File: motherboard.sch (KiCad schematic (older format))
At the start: 91 parts, among them P1 CONN_01X08, P2 CONN_01X08, U1 STM32F411-LQFP64, U10 74LS125, U11 74LS125, U12 74LS125, U13 74LS125, U14 74LS125, U15 PCA9517A, U16 PCA9517A, U2 STM32F411-LQFP64, U3 AP7313, U4 74LVC2G132, U5 FM25V20A-G, U6 FM25V20A-G, U7 FM25V20A-G, U8 FM25V20A-G, U9 74LS125, Y1 32k, Y2 8M(16pF), Y3 32k, Y4 8M(16pF)

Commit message: Added radio interrupt lines
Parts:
- removed P?: CONN_02X03, symbol CONN_02X03
- added U17: 74LS125, symbol 74LS125
- gave numbers to parts that had none: 2
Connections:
- net labels added: RADIO_RR, RADIO_RR_P, RADIO_RR_S, RADIO_TR, RADIO_TR_P, RADIO_TR_S, SGPIO_4, SGPIO_5
- net labels removed: DEP_C, DEP_NC, DEP_NO, GPIO13, GPIO14, RBF_C, RBF_NC, RBF_NO, SGPIO14, SGPIO15, SGPIO4, SGPIO5
- wire segments 264 -> 394
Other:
- moved on the sheet: C23, C24, C25, C26, P3, P4, R10, R11, R12, R13, R23, R24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

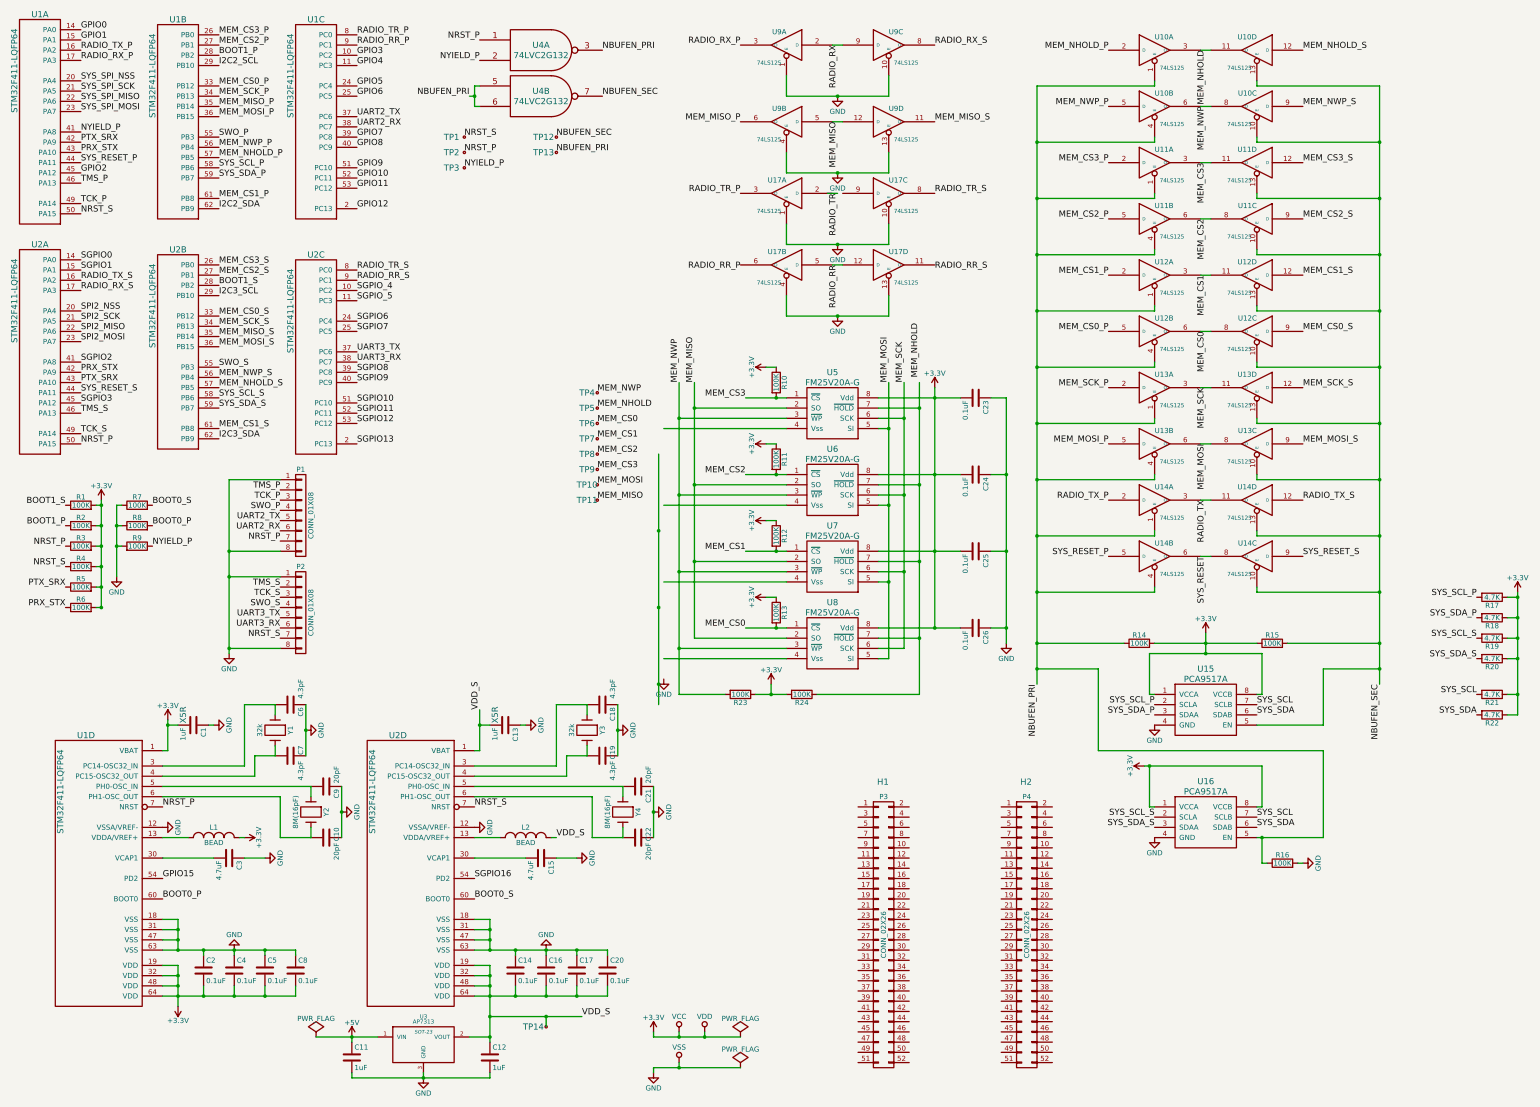
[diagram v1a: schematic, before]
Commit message: Associated symbols with footprints
Created a few modules as needed
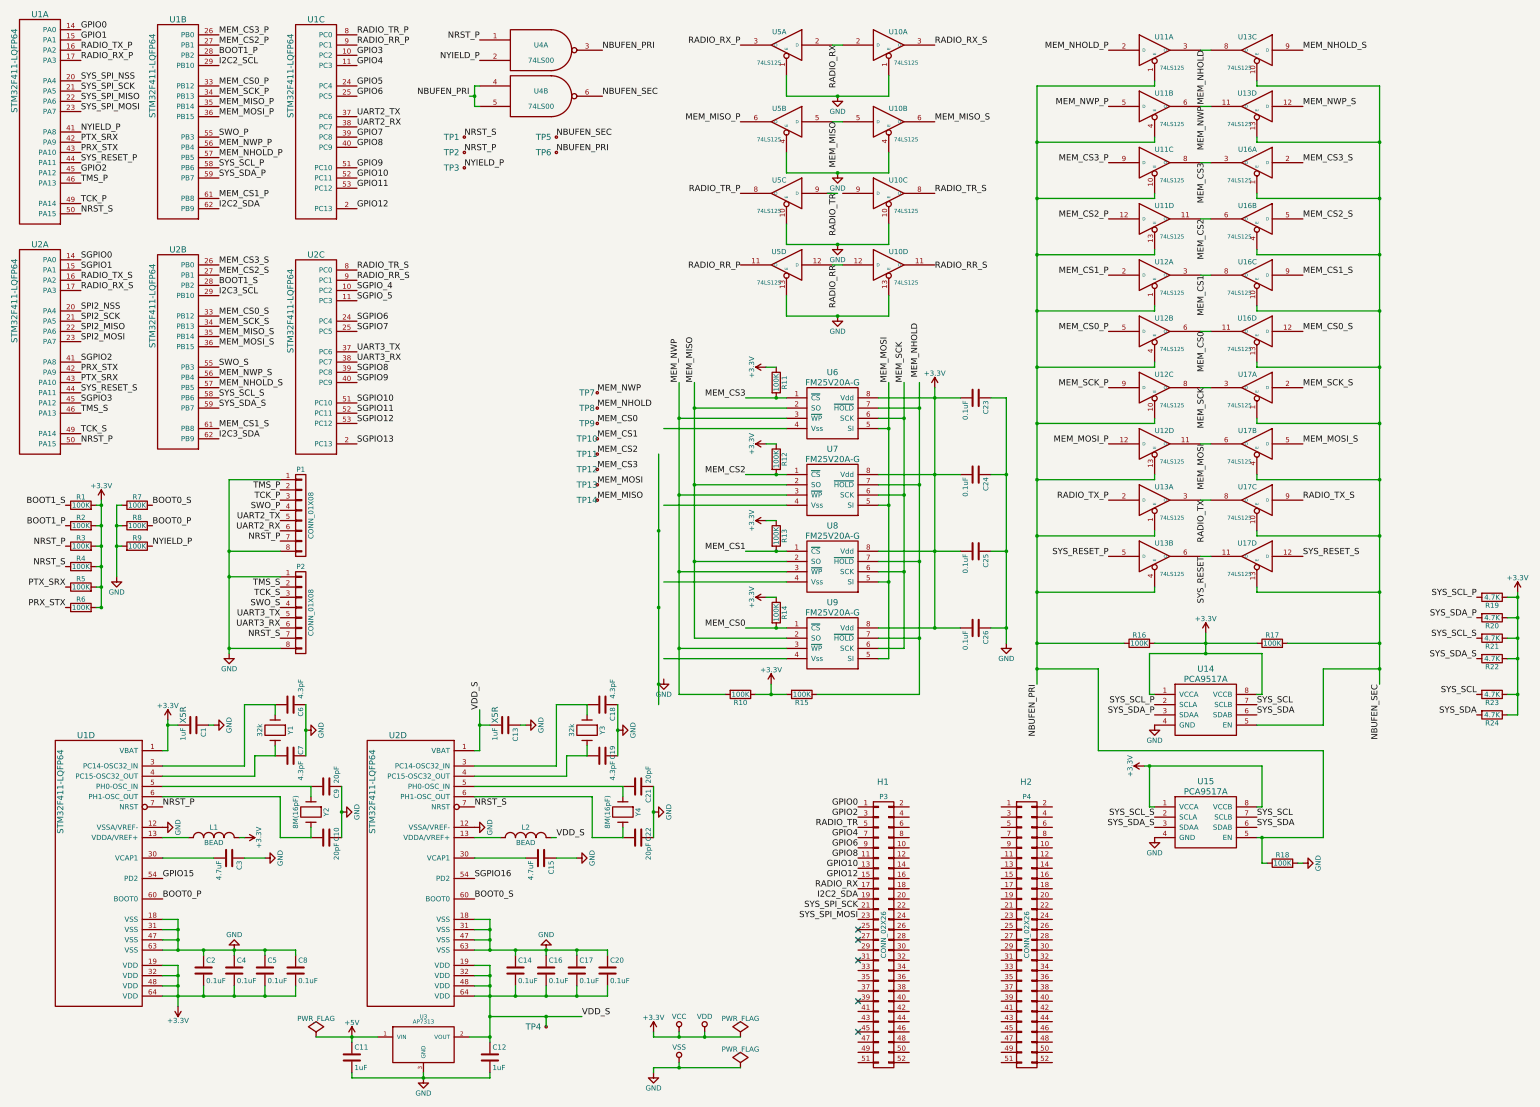
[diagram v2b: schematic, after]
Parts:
- removed U4: 74LVC2G132, symbol 74LVC2G132
- added U4: 74LS00, symbol 74LS00
- C1, C10, C11, C12, C13, C14, C15, C16, C17, C18, C19, C2, C20, C21, C22, C23, C24, C25, C26, C3, C4, C5, C6, C7, C8, C9: footprint (none) -> Capacitors_SMD:C_0805_HandSoldering
- L1, L2: footprint (none) -> Choke_SMD:Choke_SMD_1206_Handsoldering
- P1, P2: footprint (none) -> Pin_Headers:Pin_Header_Angled_1x08
- P3, P4: footprint (none) -> Socket_Strips:Socket_Strip_Straight_2x26
- R1, R2, R3, R4, R5, R6, R7, R8, R9: footprint (none) -> Resistors_SMD:R_0805_HandSoldering
- R10: renamed from R23; footprint (none) -> Resistors_SMD:R_0805_HandSoldering
- R11: renamed from R10; footprint (none) -> Resistors_SMD:R_0805_HandSoldering
- R12: renamed from R11; footprint (none) -> Resistors_SMD:R_0805_HandSoldering
- R13: renamed from R12; footprint (none) -> Resistors_SMD:R_0805_HandSoldering
- R14: renamed from R13; footprint (none) -> Resistors_SMD:R_0805_HandSoldering
- R15: renamed from R24; footprint (none) -> Resistors_SMD:R_0805_HandSoldering
- R16: renamed from R14; footprint (none) -> Resistors_SMD:R_0805_HandSoldering
- R17: renamed from R15; footprint (none) -> Resistors_SMD:R_0805_HandSoldering
- R18: renamed from R16; footprint (none) -> Resistors_SMD:R_0805_HandSoldering
- R19: renamed from R17; footprint (none) -> Resistors_SMD:R_0805_HandSoldering
- R20: renamed from R18; footprint (none) -> Resistors_SMD:R_0805_HandSoldering
- R21: renamed from R19; footprint (none) -> Resistors_SMD:R_0805_HandSoldering
- R22: renamed from R20; footprint (none) -> Resistors_SMD:R_0805_HandSoldering
- R23: renamed from R21; footprint (none) -> Resistors_SMD:R_0805_HandSoldering
- R24: renamed from R22; footprint (none) -> Resistors_SMD:R_0805_HandSoldering
- U3: footprint SOT-23 -> (none)
- renumbered TP7 to TP10, TP8 to TP11, TP9 to TP12, TP10 to TP13, TP11 to TP14, TP14 to TP4, TP12 to TP5, TP13 to TP6, TP4 to TP7, TP5 to TP8, TP6 to TP9, U9 to U10, U17 to U10, U10 to U11, U13 to U12, U14 to U13, U10 to U13, U15 to U14, U16 to U15, U11 to U16, U12 to U16, U13 to U17, U14 to U17, U9 to U5, U17 to U5, U5 to U6, U6 to U7, U7 to U8, U8 to U9
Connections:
- net +3V3: now also U4.14 (VCC), U4.14 (VCC)
- net GND: now also U10.1 (E), U10.4 (E), U5.10 (E), U5.13 (E), U4.7 (GND), U4.7 (GND); no longer U10.10 (E), U10.13 (E), U5.1 (E), U5.4 (E)
- net GPIO0: now also P3.1 (P1)
- net GPIO10: now also P3.13 (P13)
- net GPIO12: now also P3.15 (P15)
- net GPIO2: now also P3.3 (P3)
- net GPIO4: now also P3.7 (P7)
- net GPIO6: now also P3.9 (P9)
- net GPIO8: now also P3.11 (P11)
- net I2C2_SDA: now also P3.19 (P19)
- net MEM_CS0: now also U16.11 (O); no longer U16.8 (O)
- net MEM_CS0_S: now also U16.12 (D); no longer U16.9 (D)
- net MEM_CS1: now also U16.8 (O); no longer U16.11 (O)
- net MEM_CS1_S: now also U16.9 (D); no longer U16.12 (D)
- net MEM_CS2: now also U11.11 (O), U16.6 (O); no longer U11.6 (O), U16.8 (O)
- net MEM_CS2_P: now also U11.12 (D); no longer U11.5 (D)
- net MEM_CS2_S: now also U16.5 (D); no longer U16.9 (D)
- net MEM_CS3: now also U11.8 (O), U16.3 (O); no longer U11.3 (O), U16.11 (O)
- net MEM_CS3_P: now also U11.9 (D); no longer U11.2 (D)
- net MEM_CS3_S: now also U16.2 (D); no longer U16.12 (D)
- net MEM_MISO: now also U10.5 (D); no longer U10.12 (D)
- net MEM_MISO_S: now also U10.6 (O); no longer U10.11 (O)
- net MEM_MOSI: now also U12.11 (O), U17.6 (O); no longer U12.6 (O), U17.8 (O)
- net MEM_MOSI_P: now also U12.12 (D); no longer U12.5 (D)
- net MEM_MOSI_S: now also U17.5 (D); no longer U17.9 (D)
- net MEM_NHOLD: now also U13.8 (O); no longer U13.11 (O)
- net MEM_NHOLD_S: now also U13.9 (D); no longer U13.12 (D)
- net MEM_NWP: now also U13.11 (O); no longer U13.8 (O)
- net MEM_NWP_S: now also U13.12 (D); no longer U13.9 (D)
- net MEM_SCK: now also U12.8 (O), U17.3 (O); no longer U12.3 (O), U17.11 (O)
- net MEM_SCK_P: now also U12.9 (D); no longer U12.2 (D)
- net MEM_SCK_S: now also U17.2 (D); no longer U17.12 (D)
- net NBUFEN_PRI: now also U11.10 (E), U11.13 (E), U12.10 (E), U12.13 (E), U4.3, U4.4, U4.5; no longer U11.1 (E), U11.4 (E), U12.1 (E), U12.4 (E)
- net NBUFEN_SEC: now also U13.10 (E), U13.13 (E), U16.1 (E), U16.10 (E), U16.13 (E), U16.4 (E), U17.1 (E), U17.10 (E), U17.13 (E), U17.4 (E), U4.6; no longer U13.10 (E), U13.13 (E), U16.10 (E), U16.10 (E), U16.13 (E), U16.13 (E), U17.10 (E), U17.10 (E), U17.13 (E), U17.13 (E)
- net NRST_P: now also U4.1
- net NYIELD_P: now also U4.2
- net RADIO_RR: now also U5.12 (D); no longer U5.5 (D)
- net RADIO_RX: now also P3.17 (P17), U10.2 (D); no longer U10.9 (D)
- net RADIO_RX_S: now also U10.3 (O); no longer U10.8 (O)
- net RADIO_TR: now also P3.5 (P5)
- net RADIO_TR_P: now also U5.8 (O); no longer U5.3 (O)
- net RADIO_TX: now also U17.8 (O); no longer U17.11 (O)
- net RADIO_TX_S: now also U17.9 (D); no longer U17.12 (D)
- net SYS_RESET: now also U17.11 (O); no longer U17.8 (O)
- net SYS_RESET_S: now also U17.12 (D); no longer U17.9 (D)
- net SYS_SPI_MOSI: now also P3.23 (P23)
- net SYS_SPI_SCK: now also P3.21 (P21)
- no-connect marks 0 -> 5

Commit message: Design rules
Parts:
- TP1, TP10, TP11, TP12, TP13, TP14, TP2, TP3, TP4, TP5, TP6, TP7, TP8, TP9: footprint (none) -> motherboard:TP_0603
- U1, U2: footprint (none) -> Housings_QFP:LQFP-64_10x10mm_Pitch0.5mm
- U10, U11, U12, U13, U16, U17, U4, U5: footprint (none) -> Housings_SOIC:SOIC-14_3.9x8.7mm_Pitch1.27mm
- U14, U15, U6, U7, U8, U9: footprint (none) -> Housings_SOIC:SOIC-8_3.9x4.9mm_Pitch1.27mm
- U3: footprint (none) -> TO_SOT_Packages_SMD:SOT-23_Handsoldering
- Y1, Y3: footprint (none) -> motherboard:SOJ-4_5.5mm
- Y2, Y4: footprint (none) -> motherboard:SOJ-4_9.4mm

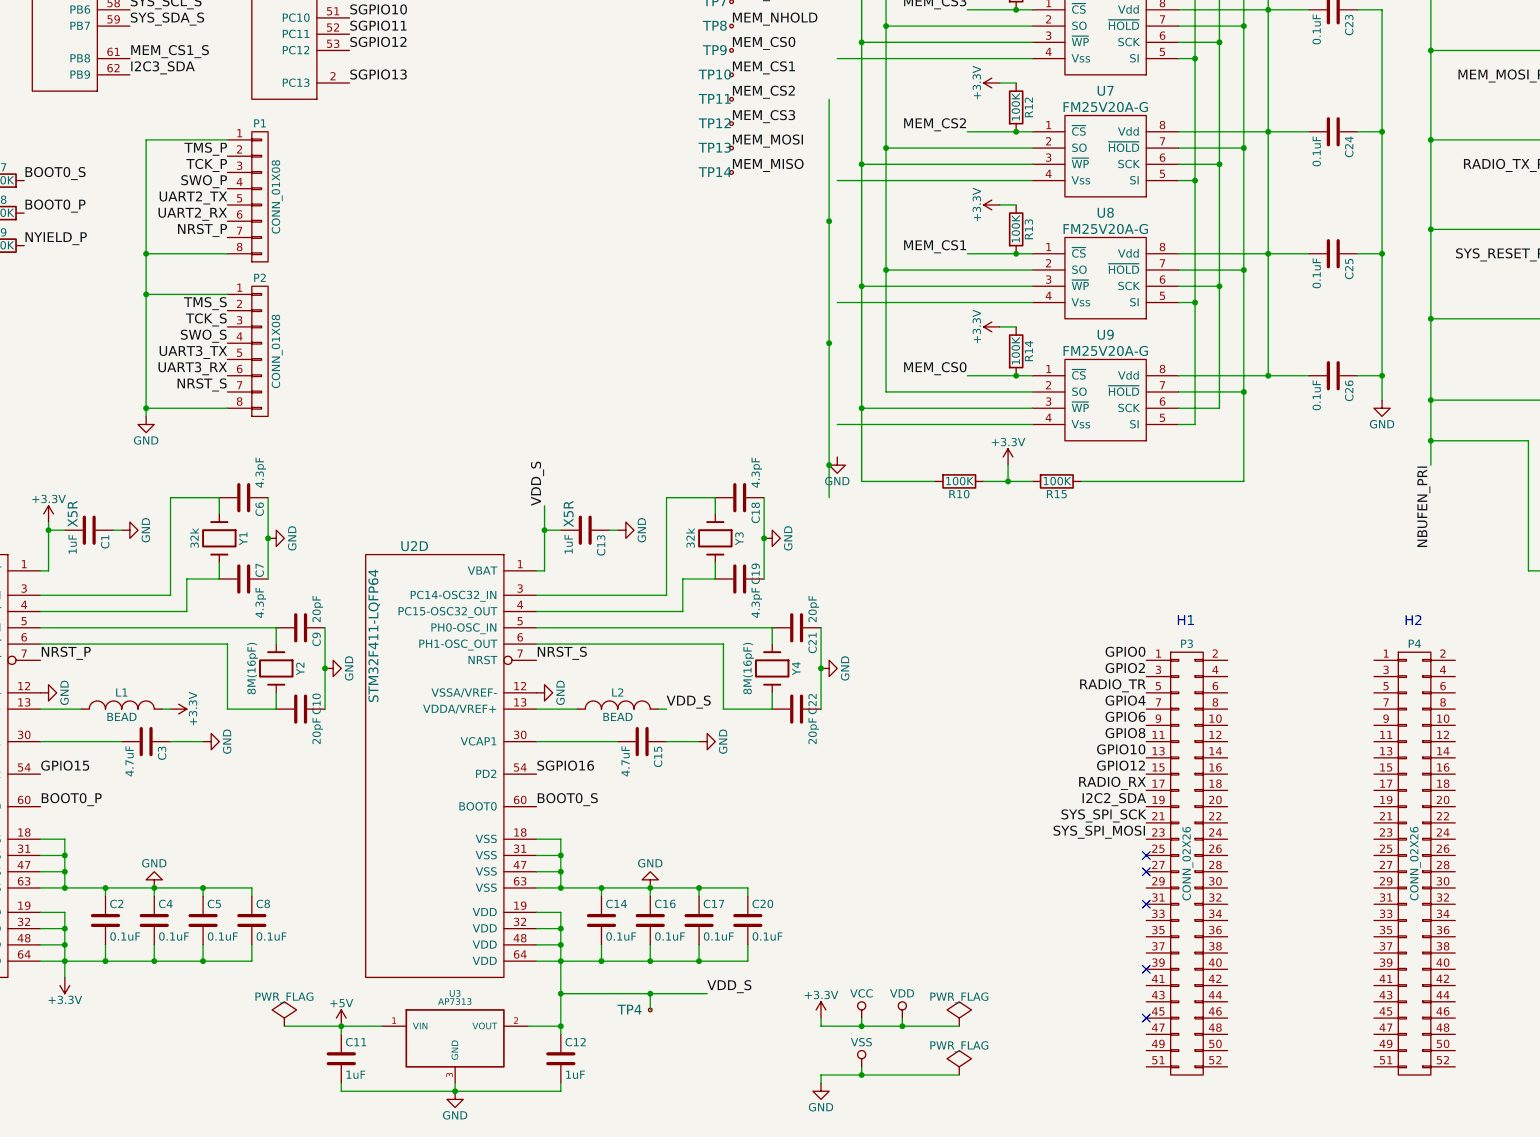
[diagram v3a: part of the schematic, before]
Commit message: Finished board outline and connector placement
Beginning to assign GPIOs and layout components
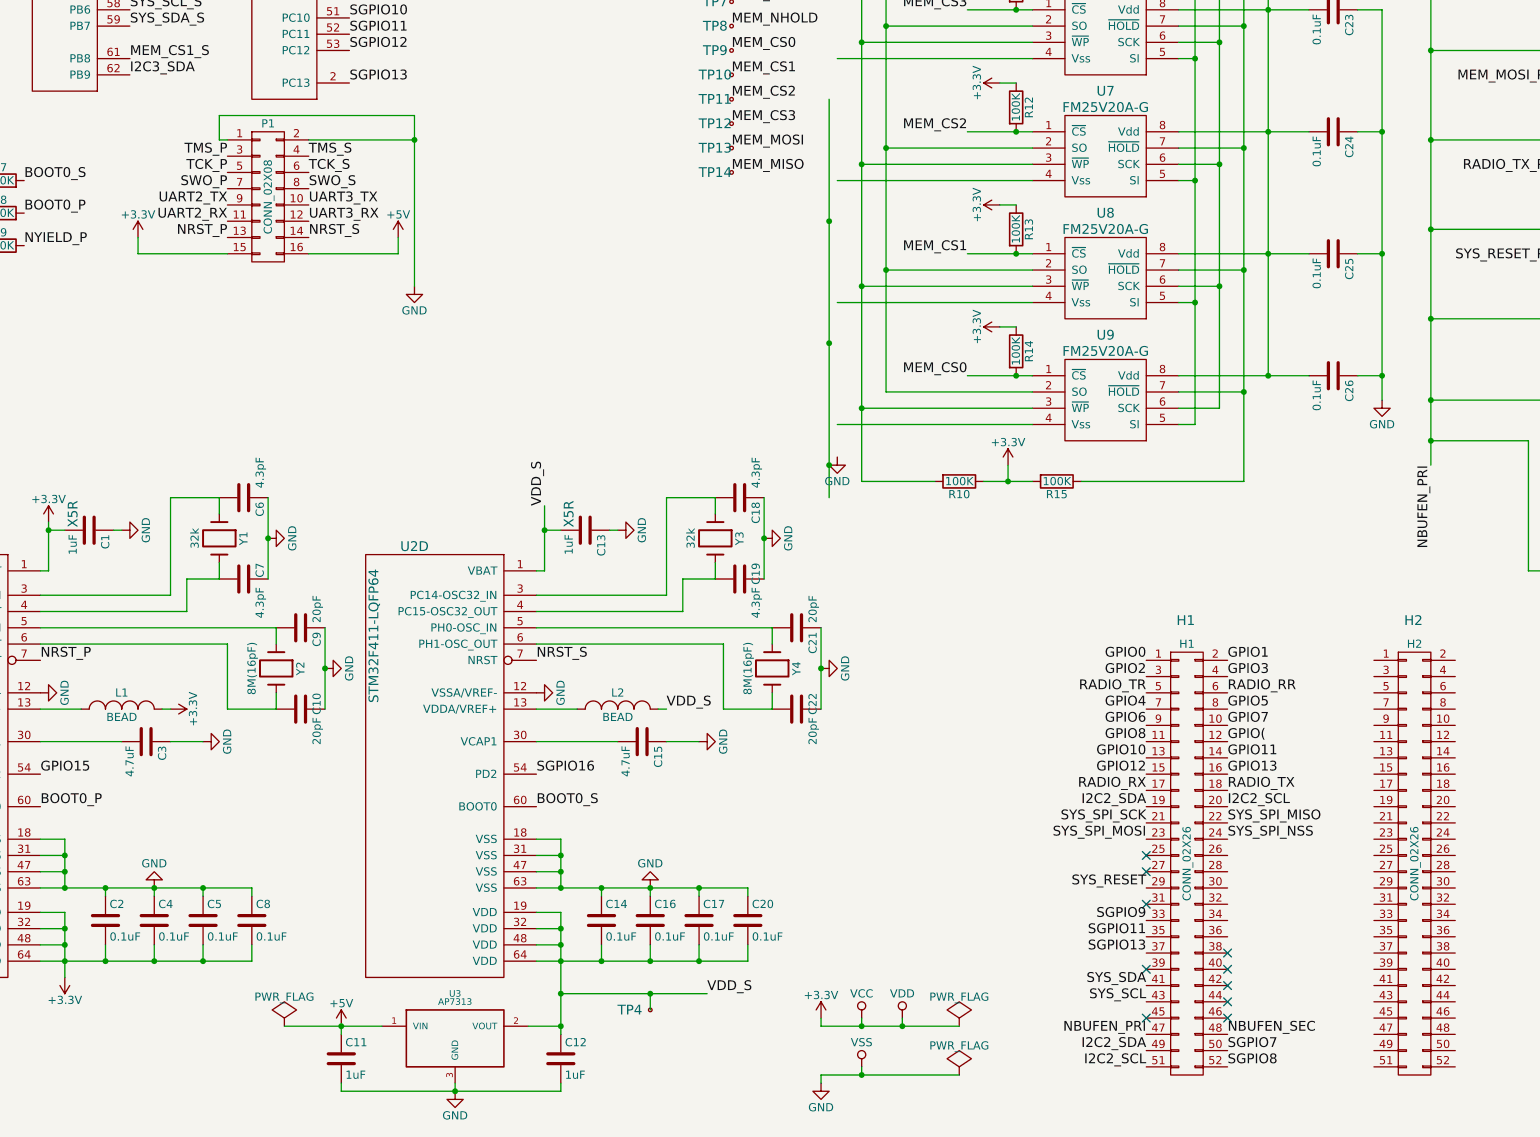
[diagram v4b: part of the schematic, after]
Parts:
- removed P1, P2: CONN_01X08, Pin_Headers:Pin_Header_Angled_1x08, symbol CONN_01X08
- added P1: CONN_02X08, Pin_Headers:Pin_Header_Angled_2x08, symbol CONN_02X08
- renumbered P3 to H1, P4 to H2
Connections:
- net +3V3: now also P1.15 (P15)
- net +5V: now also P1.16 (P16)
- net GND: now also P1.1 (P1), P1.2 (P2)
- net GPIO1: now also H1.2 (P2)
- net GPIO11: now also H1.14 (P14)
- net GPIO3: now also H1.4 (P4)
- net GPIO5: now also H1.8 (P8)
- net GPIO7: now also H1.10 (P10)
- net I2C2_SCL: now also H1.20 (P20), H1.51 (P51)
- net I2C2_SDA: now also H1.49 (P49)
- net NBUFEN_PRI: now also H1.47 (P47)
- net NBUFEN_SEC: now also H1.48 (P48)
- net NRST_P: now also P1.13 (P13)
- net NRST_S: now also P1.14 (P14)
- net RADIO_RR: now also H1.6 (P6)
- net RADIO_TX: now also H1.18 (P18)
- net SGPIO11: now also H1.35 (P35)
- net SGPIO13: now also H1.37 (P37)
- net SGPIO7: now also H1.50 (P50)
- net SGPIO8: now also H1.52 (P52)
- net SGPIO9: now also H1.33 (P33)
- net SWO_P: now also P1.7 (P7)
- net SWO_S: now also P1.8 (P8)
- net SYS_RESET: now also H1.29 (P29)
- net SYS_SCL: now also H1.43 (P43)
- net SYS_SDA: now also H1.41 (P41)
- net SYS_SPI_MISO: now also H1.22 (P22)
- net SYS_SPI_NSS: now also H1.24 (P24)
- net TCK_P: now also P1.5 (P5)
- net TCK_S: now also P1.6 (P6)
- net TMS_P: now also P1.3 (P3)
- net TMS_S: now also P1.4 (P4)
- net UART2_RX: now also P1.11 (P11)
- net UART2_TX: now also P1.9 (P9)
- net UART3_RX: now also P1.12 (P12)
- net UART3_TX: now also P1.10 (P10)
- net GPIO(: now reaches H1.12 (P12)
- net GPIO13: now reaches H1.16 (P16)
- no-connect marks 5 -> 10
